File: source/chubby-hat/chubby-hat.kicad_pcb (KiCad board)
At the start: 2 copper layers, 143.5 x 91.4 mm, 148 parts, among them J1 RP2040.SWD, J10 USB_C_Receptacle_USB2.0, J11 HUB75, J12 HUB75, J13 HUB75, J14 v7.0, J15 v8.0, J16 HUB75, J17 Conn_01x02, J18 HUB75, J19 HUB75, J2 Conn_ARM_JTAG_SWD_10, J20 V7.0, J21 V8.0, J22 HUB75, J23 HUB75, J3 Conn_ARM_JTAG_SWD_10, J4 TC2030, J5 UART, J6 5V, J7 5V, J8 5V, J9 5V, Q1 BC807DS,115, Q2 AO3401A, Q3 BC807DS,115, Q4 AO3401A, SW1 RUN, SW2 BOOT, U1 AMS1117-3.3, U2 RP2040-Zero, U3 USBLC6-2SC6, U4 P25Q40H-SSH-IT, U5 RP2040, Y1 12M

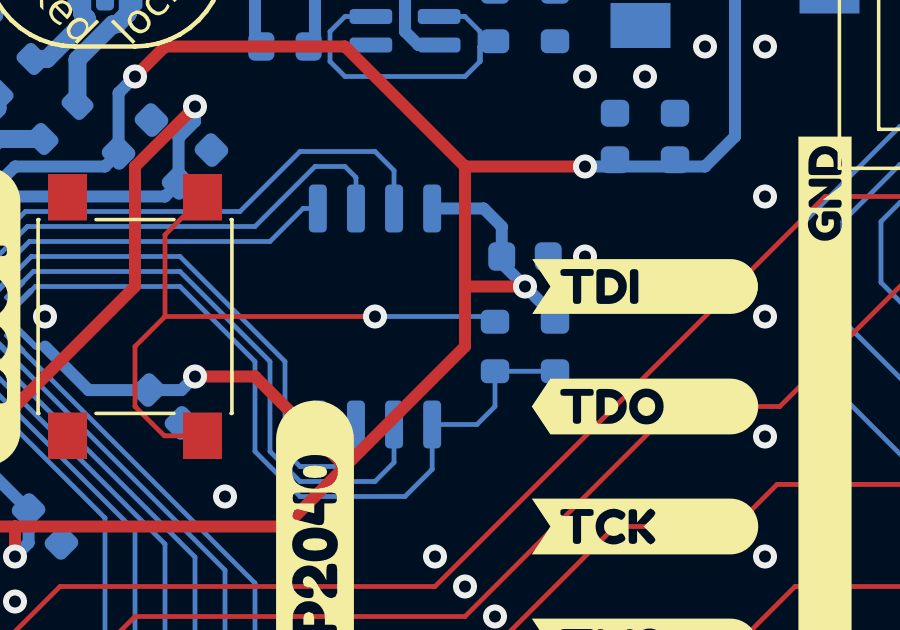
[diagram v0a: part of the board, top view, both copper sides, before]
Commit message: add USON-8 footprint for W25Q16JV style flash; closes #13
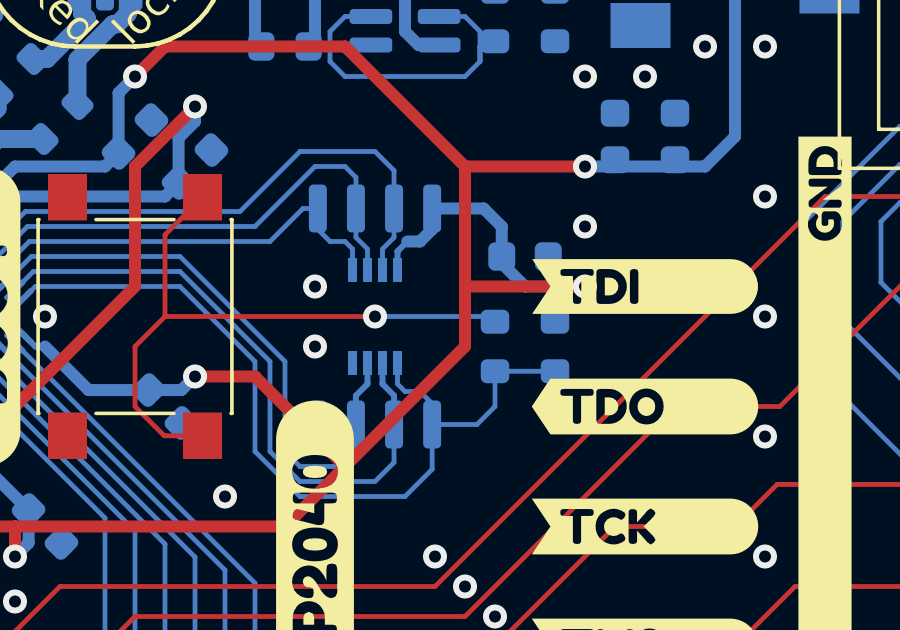
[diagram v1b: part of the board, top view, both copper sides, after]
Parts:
- added U6: W25Q16JV, Package_SO:VSSOP-8_2.3x2mm_P0.5mm, B.Cu at (173.0, 80.0)
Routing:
- net +3V3: track 449.1 -> 455.5 mm
- net /RP2040/QSPI.~{CS}: track 25.9 -> 28.7 mm
- net /RP2040/QSPI.IO0: track 11.6 -> 14.4 mm
- net /RP2040/QSPI.IO3: track 16.8 -> 19.0 mm
- net /RP2040/QSPI.IO2: track 17.9 -> 20.1 mm
- net /RP2040/QSPI.IO1: track 19.1 -> 21.3 mm
- net /RP2040/QSPI.CLK: track 14.8 -> 17.0 mm
- net GND: vias 108 -> 110
